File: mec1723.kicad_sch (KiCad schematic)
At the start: 87 parts, among them J10 PinHeader_2x5_P1.27mm_SMD, J11 PinHeader_2x5_P1.27mm_SMD, J12 PinHeader_2x5_P1.27mm_SMD, J2 PinHeader_2x5_P1.27mm_SMD, J3 PinHeader_2x5_P1.27mm_SMD, J4 PinHeader_2x5_P1.27mm_SMD, J5 PinHeader_2x5_P1.27mm_SMD, J6 PinHeader_2x5_P1.27mm_SMD, J7 PinHeader_2x5_P1.27mm_SMD, J8 PinHeader_2x5_P1.27mm_SMD, J9 PinHeader_2x5_P1.27mm_SMD, SW1 SW_KSC441J70SHLFS_SMD, SW2 SW_KSC441J70SHLFS_SMD, SW3 SW_KSC441J70SHLFS_SMD, U1 MEC1723N-B0-I/SZ, Y1 Resonator_32.768kHz_ECX-31B

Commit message: [#103697] Initial wider fanout
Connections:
- net 32kHz_IN: no longer J11.7
- net 32kHz_OUT: no longer J11.9
- net 7SEG_L.A: now also U1.L2 (GPIO067/VREF2_ADC); no longer U1.L1 (GPIO206/ADC06)
- net 7SEG_L.B: now also U1.L1 (GPIO206/ADC06); no longer U1.L2 (GPIO067/VREF2_ADC)
- net 7SEG_L.C: now also U1.J2 (GPIO202/ADC02/TRACEDATA2); no longer U1.J1 (GPIO203/ADC03/TRACEDATA3)
- net 7SEG_L.E: now also U1.J1 (GPIO203/ADC03/TRACEDATA3); no longer U1.J2 (GPIO202/ADC02/TRACEDATA2)
- net BGP00: no longer J12.1
- net BGP01: no longer J11.8
- net BGP02: no longer J11.10
- net GPIO043: no longer U1.G13 (GPIO240)
- net PECI_DAT: no longer J12.9
- net PWRGD_S0iX: no longer J12.3
- net SLP_S0#: no longer J12.7
- net VCI_OUT2: no longer J11.3
- net VCI_OVRD_IN: no longer J11.1
- net GPIO156: now reaches U1.A13 (GPIO156/LED0)
- net GPIO157: now reaches U1.B13 (GPIO157/LED1)
- net GPIO241: now reaches U1.B8 (GPIO241/CMP_VOUT0/PWM0_ALT)
- net GPIO254: now reaches U1.B9 (GPIO254)
- net GPIO153: now reaches U1.C12 (GPIO153/LED2)
- net GPIO175: now reaches U1.C13 (GPIO175/CMP_VOUT1/PWM8_ALT)
- net GPIO135: now reaches U1.E13 (GPIO035/PWM8/CTOUT1/ICT15/LED3)
- net GPIO151: now reaches U1.L9 (GPIO151/ICT4/KSO15)
- net GPIO152: now reaches U1.N10 (GPIO152/KSO14/GPTP_OUT3/I2C07_SDA_ALT)
- new net GPIO240: U1.G13 (GPIO240)

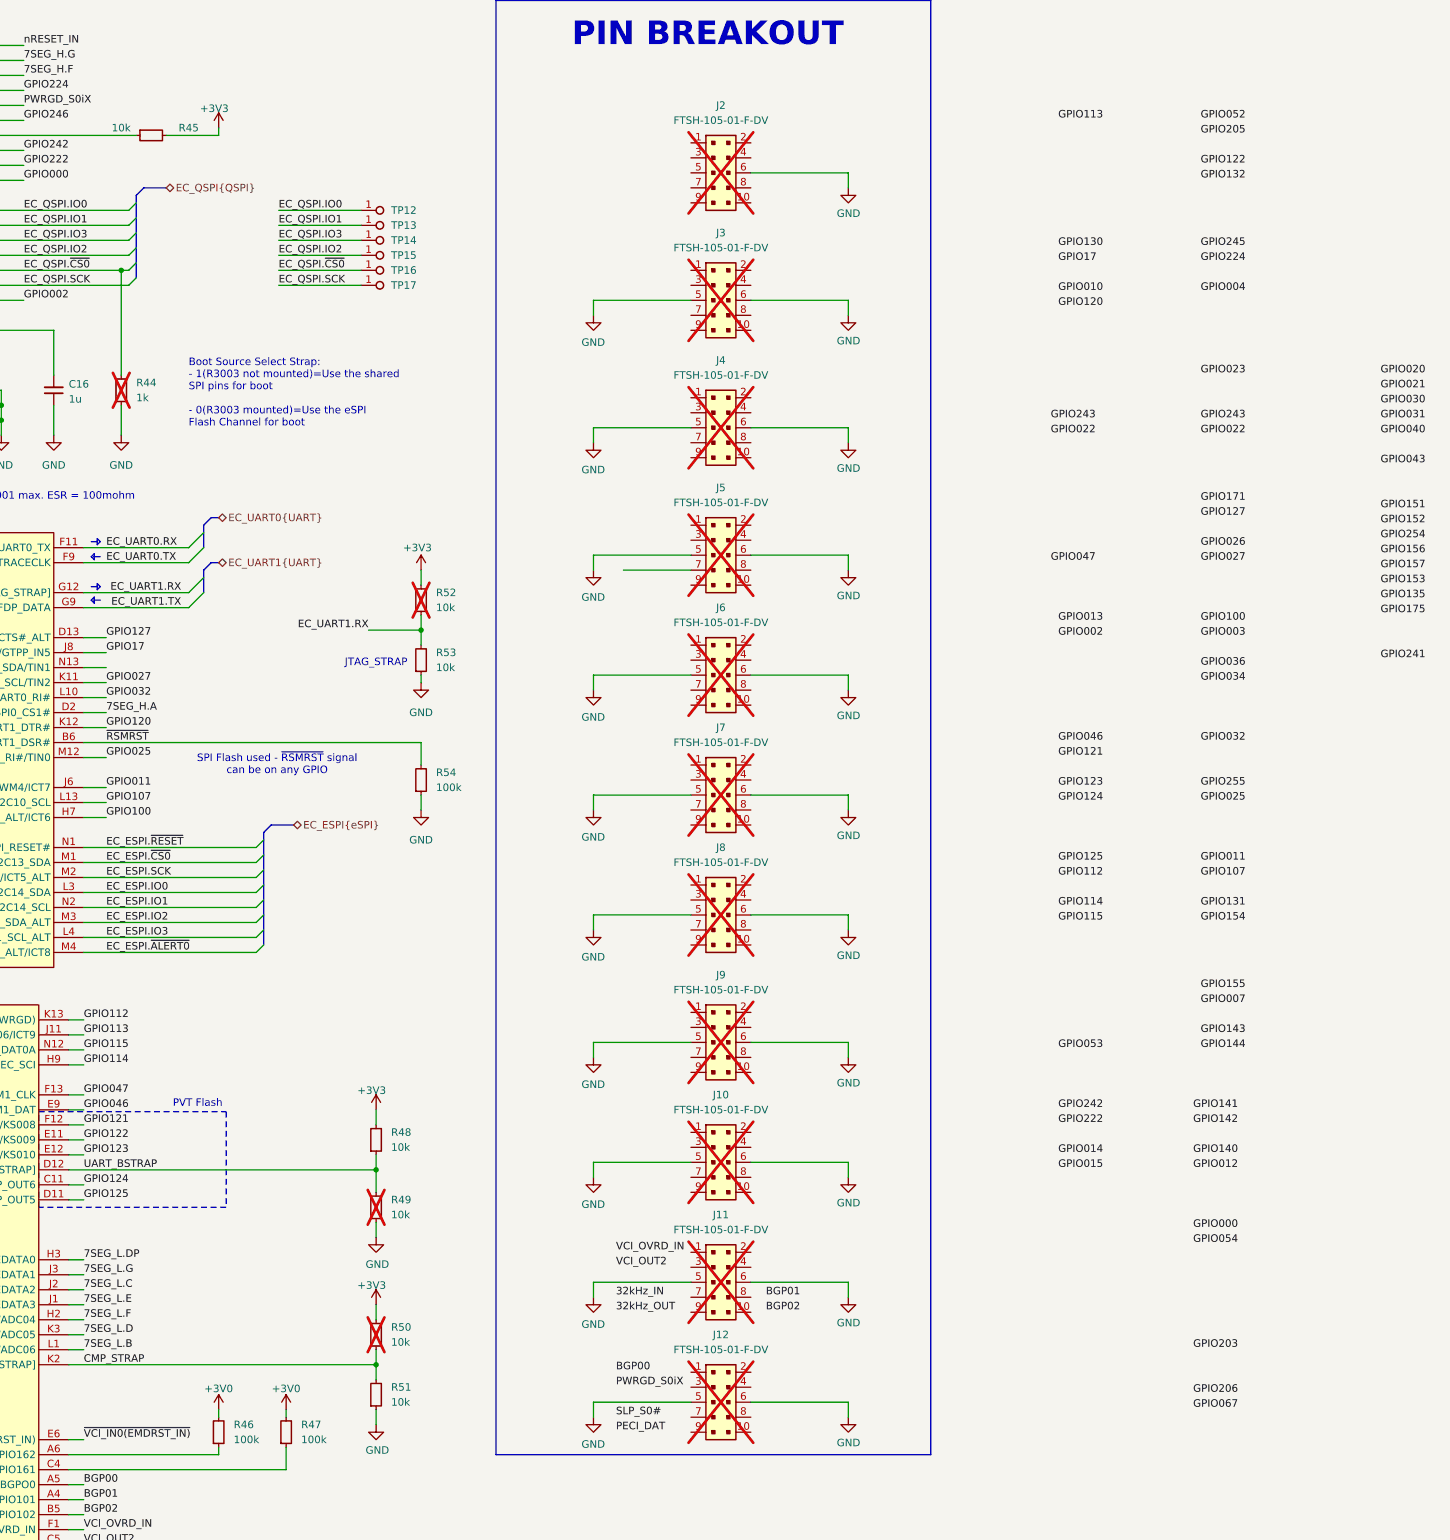
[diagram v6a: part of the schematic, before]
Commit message: [#103697] Route all traces on PCB
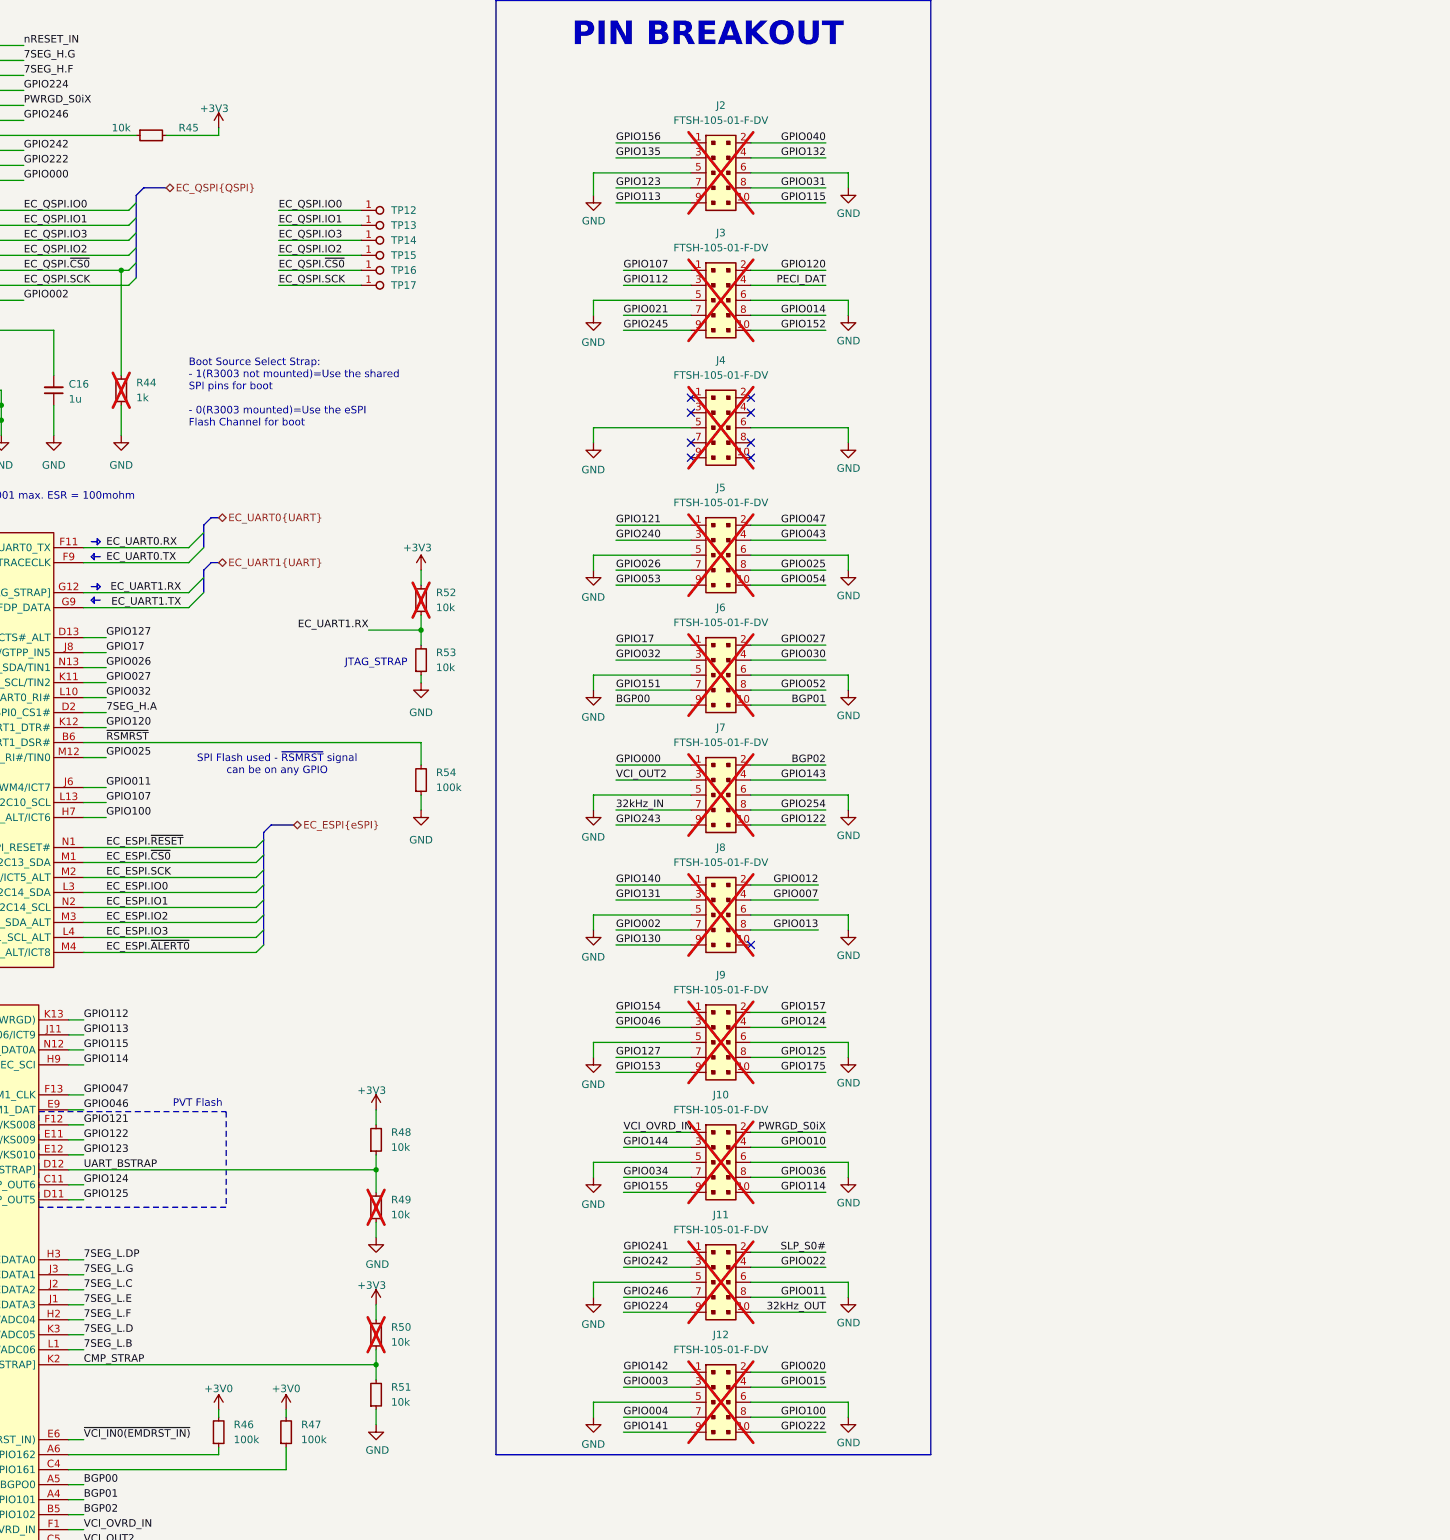
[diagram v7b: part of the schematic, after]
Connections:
- net 32kHz_IN: now also J7.7
- net 32kHz_OUT: now also J11.10
- net BGP00: now also J6.9
- net BGP01: now also J6.10
- net BGP02: now also J7.2
- net GND: now also J2.5
- net GPIO000: now also J7.1
- net GPIO002: now also J8.7
- net GPIO003: now also J12.3
- net GPIO004: now also J12.7
- net GPIO007: now also J8.4
- net GPIO010: now also J10.4
- net GPIO011: now also J11.8
- net GPIO012: now also J8.2
- net GPIO013: now also J8.8
- net GPIO014: now also J3.8
- net GPIO015: now also J12.4
- net GPIO020: now also J12.2
- net GPIO021: now also J3.7
- net GPIO022: now also J11.4
- net GPIO025: now also J5.8
- net GPIO026: now also J5.7, U1.N13 (GPIO026/KSI3/UART0_DTR#/I2C12_SDA/TIN1)
- net GPIO027: now also J6.2
- net GPIO030: now also J6.4
- net GPIO031: now also J2.8
- net GPIO032: now also J6.3
- net GPIO034: now also J10.7
- net GPIO036: now also J10.8
- net GPIO040: now also J2.2
- net GPIO043: now also J5.4
- net GPIO046: now also J9.3
- net GPIO047: now also J5.2
- net GPIO052: now also J6.8
- net GPIO053: now also J5.9
- net GPIO054: now also J5.10
- net GPIO100: now also J12.8
- net GPIO107: now also J3.1
- net GPIO112: now also J3.3
- net GPIO113: now also J2.9
- net GPIO114: now also J10.10
- net GPIO115: now also J2.10
- net GPIO120: now also J3.2
- net GPIO121: now also J5.1
- net GPIO122: now also J7.10
- net GPIO123: now also J2.7
- net GPIO124: now also J9.4
- net GPIO125: now also J9.8
- net GPIO127: now also J9.7
- net GPIO130: now also J8.9
- net GPIO131: now also J8.3
- net GPIO132: now also J2.4
- net GPIO135: now also J2.3
- net GPIO140: now also J8.1
- net GPIO141: now also J12.9
- net GPIO142: now also J12.1
- net GPIO143: now also J7.4
- net GPIO144: now also J10.3
- net GPIO151: now also J6.7
- net GPIO152: now also J3.10
- net GPIO153: now also J9.9
- net GPIO154: now also J9.1
- net GPIO155: now also J10.9
- net GPIO156: now also J2.1
- net GPIO157: now also J9.2
- net GPIO17: now also J6.1
- net GPIO175: now also J9.10
- net GPIO222: now also J12.10
- net GPIO224: now also J11.9
- net GPIO240: now also J5.3
- net GPIO241: now also J11.1
- net GPIO242: now also J11.3
- net GPIO243: now also J7.9
- net GPIO245: now also J3.9
- net GPIO246: now also J11.7
- net GPIO254: now also J7.8
- net PECI_DAT: now also J3.4
- net PWRGD_S0iX: now also J10.2
- net SLP_S0#: now also J11.2
- net VCI_OUT2: now also J7.3
- net VCI_OVRD_IN: now also J10.1
- no-connect marks 0 -> 9
